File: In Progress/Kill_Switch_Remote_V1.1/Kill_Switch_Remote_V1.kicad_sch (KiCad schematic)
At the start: 56 parts, among them J1 USB_B_Micro, J2 S2B-PH-K-S(LF)(SN), J3 U.FL-R-SMT-1(10), Q2 UMH3N, SW4 AS11CH, U1 ESP32-PICO-MINI-02, U2 CP2102N-A02-GQFN28, U3 LP5912-3.3DRV, U4 MCP73871-2CC-Custom, U5 RFM95W-915S2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

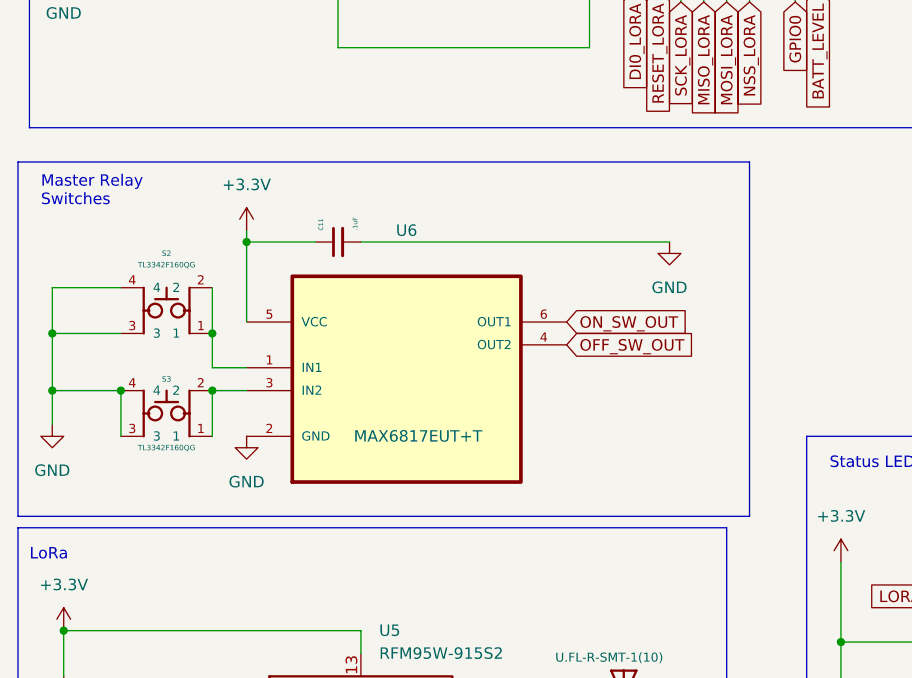
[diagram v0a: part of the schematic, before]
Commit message: Updating the Kill Switch Droid side
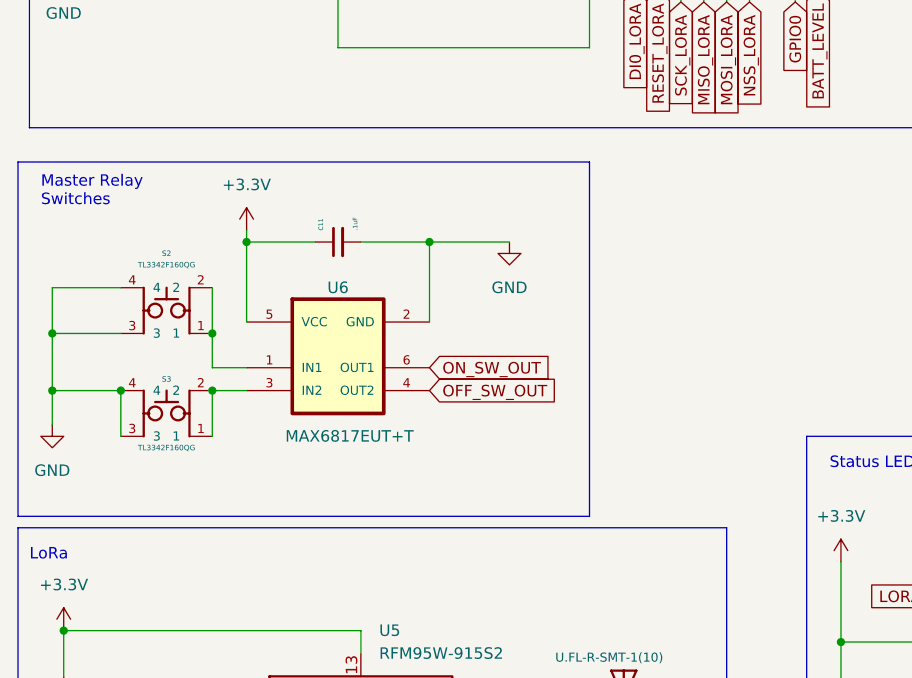
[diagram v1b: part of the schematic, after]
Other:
- moved on the sheet: U6
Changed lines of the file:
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@@
   (junction (at 104.14 152.4) (diameter 0) (color 0 0 0 0)
   )
+  (junction (at 58.42 107.95) (diameter 0) (color 0 0 0 0)
+  )
   (junction (at 35.56 68.58) (diameter 0) (color 0 0 0 0)
   )
@@
     (stroke (width 0) (type default) (color 0 0 0 0))
   )
-  (polyline (pts (xy 12.7 99.06) (xy 93.98 99.06))
+  (polyline (pts (xy 12.7 99.06) (xy 76.2 99.06))
     (stroke (width 0) (type default) (color 0 0 0 0))
   )
@@
     (stroke (width 0) (type default) (color 0 0 0 0))
   )
+  (wire (pts (xy 58.42 107.95) (xy 67.31 107.95))
+    (stroke (width 0) (type default) (color 0 0 0 0))
+  )
   (wire (pts (xy 237.49 66.04) (xy 237.49 71.12))
     (stroke (width 0) (type default) (color 0 0 0 0))
@@
     (stroke (width 0) (type default) (color 0 0 0 0))
   )
+  (wire (pts (xy 58.42 107.95) (xy 58.42 116.84))
+    (stroke (width 0) (type default) (color 0 0 0 0))
+  )
   (wire (pts (xy 48.26 21.59) (xy 48.26 36.83))
     (stroke (width 0) (type default) (color 0 0 0 0))
@@
     (stroke (width 0) (type default) (color 0 0 0 0))
   )
-  (polyline (pts (xy 12.7 138.43) (xy 93.98 138.43))
+  (polyline (pts (xy 12.7 138.43) (xy 76.2 138.43))
     (stroke (width 0) (type default) (color 0 0 0 0))
   )
@@
     (stroke (width 0) (type default) (color 0 0 0 0))
   )
-  (wire (pts (xy 50.8 107.95) (xy 85.09 107.95))
+  (wire (pts (xy 50.8 107.95) (xy 58.42 107.95))
     (stroke (width 0) (type default) (color 0 0 0 0))
   )
@@
     (stroke (width 0) (type default) (color 0 0 0 0))
   )
-  (polyline (pts (xy 93.98 138.43) (xy 93.98 99.06))
+  (polyline (pts (xy 76.2 138.43) (xy 76.2 99.06))
     (stroke (width 0) (type default) (color 0 0 0 0))
   )
@@
     )
   )
-  (global_label "OFF_SW_OUT" (shape input) (at 73.66 119.38 0) (fields_autoplaced)
+  (global_label "OFF_SW_OUT" (shape input) (at 58.42 124.46 0) (fields_autoplaced)
     (effects (font (size 1.27 1.27)) (justify left))
-    (property "Intersheet References" "${INTERSHEET_REFS}" (id 0) (at 87.8055 119.3006 0)
+    (property "Intersheet References" "${INTERSHEET_REFS}" (id 0) (at 72.5655 124.3806 0)
       (effects (font (size 1.27 1.27)) (justify left) hide)
     )
@@
     )
   )
-  (global_label "ON_SW_OUT" (shape input) (at 73.66 116.84 0) (fields_autoplaced)
+  (global_label "ON_SW_OUT" (shape input) (at 58.42 121.92 0) (fields_autoplaced)
     (effects (font (size 1.27 1.27)) (justify left))
-    (property "Intersheet References" "${INTERSHEET_REFS}" (id 0) (at 86.9588 116.7606 0)
+    (property "Intersheet References" "${INTERSHEET_REFS}" (id 0) (at 71.7188 121.8406 0)
       (effects (font (size 1.27 1.27)) (justify left) hide)
     )
@@
     (pin "2")
   )
-  (symbol (lib_id "power:GND") (at 38.1 129.54 0) (unit 1)
-    (in_bom yes) (on_board yes) (fields_autoplaced)
-    (property "Reference" "#PWR0143" (id 0) (at 38.1 135.89 0)
-      (effects (font (size 1.27 1.27)) hide)
-    )
-    (property "Value" "GND" (id 1) (at 38.1 134.62 0))
-    (property "Footprint" "" (id 2) (at 38.1 129.54 0)
-      (effects (font (size 1.27 1.27)) hide)
-    )
-    (property "Datasheet" "" (id 3) (at 38.1 129.54 0)
-      (effects (font (size 1.27 1.27)) hide)
-    )
-    (pin "1")
-  )
   (symbol (lib_id "power:GND") (at 151.13 172.72 0) (unit 1)
     (in_bom yes) (on_board yes)
@@
     (pin "1")
   )
-  (symbol (lib_id "Custom:MAX6817EUT+T") (at 55.88 119.38 0) (unit 1)
+  (symbol (lib_id "Custom:MAX6817EUT+T") (at 48.26 119.38 0) (unit 1)
     (in_bom yes) (on_board yes)
-    (property "Reference" "U6" (id 0) (at 55.88 106.68 0))
-    (property "Value" "MAX6817EUT+T" (id 1) (at 57.15 129.54 0))
-    (property "Footprint" "SOT95P280X145-6N" (id 2) (at 55.88 119.38 0)
+    (property "Reference" "U6" (id 0) (at 48.26 113.03 0))
+    (property "Value" "MAX6817EUT+T" (id 1) (at 49.53 129.54 0))
+    (property "Footprint" "SOT95P280X145-6N" (id 2) (at 48.26 119.38 0)
       (effects (font (size 1.27 1.27)) (justify bottom) hide)
     )
-    (property "Datasheet" "https://www.analog.com/media/en/technical-documentation/data-sheets/MAX6816-MAX6818.pdf" (id 3) (at 55.88 119.38 0)
+    (property "Datasheet" "https://www.analog.com/media/en/technical-documentation/data-sheets/MAX6816-MAX6818.pdf" (id 3) (at 48.26 119.38 0)
       (effects (font (size 1.27 1.27)) hide)
     )
-    (property "PACKAGE" "SOT23-6" (id 4) (at 55.88 119.38 0)
+    (property "PACKAGE" "SOT23-6" (id 4) (at 48.26 119.38 0)
       (effects (font (size 1.27 1.27)) (justify bottom) hide)
     )
-    (property "MPN" "MAX6817EUT+T" (id 5) (at 55.88 119.38 0)
+    (property "MPN" "MAX6817EUT+T" (id 5) (at 48.26 119.38 0)
       (effects (font (size 1.27 1.27)) (justify bottom) hide)
     )
-    (property "OC_NEWARK" "68K9458" (id 6) (at 55.88 119.38 0)
+    (property "OC_NEWARK" "68K9458" (id 6) (at 48.26 119.38 0)
       (effects (font (size 1.27 1.27)) (justify bottom) hide)
     )
-    (property "OC_FARNELL" "1299771" (id 7) (at 55.88 119.38 0)
+    (property "OC_FARNELL" "1299771" (id 7) (at 48.26 119.38 0)
       (effects (font (size 1.27 1.27)) (justify bottom) hide)
     )
-    (property "SUPPLIER" "Maxim" (id 8) (at 55.88 119.38 0)
+    (property "SUPPLIER" "Maxim" (id 8) (at 48.26 119.38 0)
       (effects (font (size 1.27 1.27)) (justify bottom) hide)
     )
@@
     (pin "2")
   )
-  (symbol (lib_id "power:GND") (at 85.09 107.95 0) (unit 1)
+  (symbol (lib_id "power:GND") (at 67.31 107.95 0) (unit 1)
     (in_bom yes) (on_board yes) (fields_autoplaced)
-    (property "Reference" "#PWR0127" (id 0) (at 85.09 114.3 0)
+    (property "Reference" "#PWR0127" (id 0) (at 67.31 114.3 0)
       (effects (font (size 1.27 1.27)) hide)
     )
-    (property "Value" "GND" (id 1) (at 85.09 113.03 0))
-    (property "Footprint" "" (id 2) (at 85.09 107.95 0)
+    (property "Value" "GND" (id 1) (at 67.31 113.03 0))
+    (property "Footprint" "" (id 2) (at 67.31 107.95 0)
       (effects (font (size 1.27 1.27)) hide)
     )
-    (property "Datasheet" "" (id 3) (at 85.09 107.95 0)
+    (property "Datasheet" "" (id 3) (at 67.31 107.95 0)
       (effects (font (size 1.27 1.27)) hide)
     )
@@
       (reference "#PWR0142") (unit 1) (value "GND") (footprint "")
     )
-    (path "/29c27ba3-a492-44ef-9417-774b5144448a"
-      (reference "#PWR0143") (unit 1) (value "GND") (footprint "")
-    )
     (path "/1e10f6a7-f66e-43cd-a1bd-d7754ef94760"

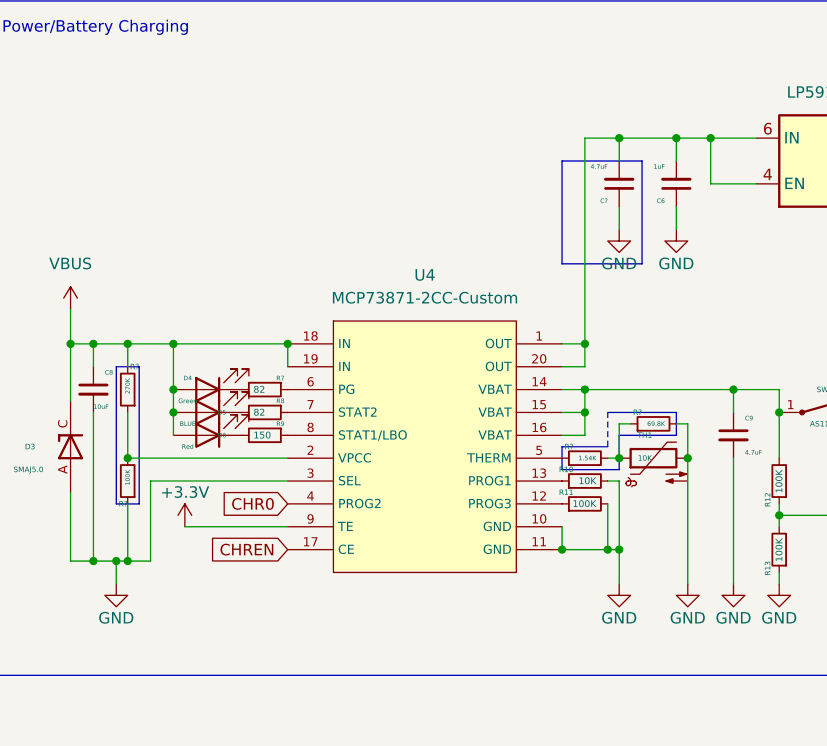
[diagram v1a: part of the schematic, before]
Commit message: Updates to the kill switches
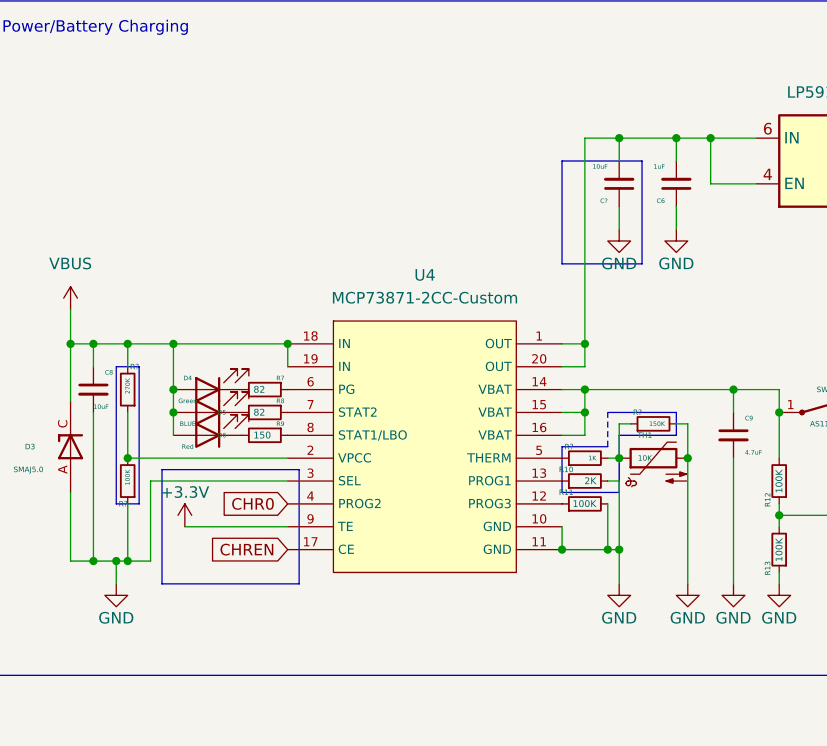
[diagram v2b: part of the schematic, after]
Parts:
- C?: value 4.7uF -> 10uF
- R10: value 10K -> 2K
- R?: value 1.54K -> 1K
- R?: value 69.8K -> 150K
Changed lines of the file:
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@@
     (stroke (width 0) (type default) (color 0 0 0 0))
   )
-  (polyline (pts (xy 231.14 140.97) (xy 224.79 140.97))
+  (polyline (pts (xy 231.14 143.51) (xy 224.79 143.51))
     (stroke (width 0) (type default) (color 0 0 0 0))
   )
@@
     (stroke (width 0) (type default) (color 0 0 0 0))
   )
+  (polyline (pts (xy 195.58 153.67) (xy 195.58 140.97))
+    (stroke (width 0) (type default) (color 0 0 0 0))
+  )
   (wire (pts (xy 232.41 77.47) (xy 232.41 80.01))
     (stroke (width 0) (type default) (color 0 0 0 0))
@@
     (stroke (width 0) (type default) (color 0 0 0 0))
   )
+  (polyline (pts (xy 180.34 142.24) (xy 180.34 140.97))
+    (stroke (width 0) (type default) (color 0 0 0 0))
+  )
   (wire (pts (xy 21.59 41.91) (xy 21.59 46.99))
     (stroke (width 0) (type default) (color 0 0 0 0))
@@
     (stroke (width 0) (type default) (color 0 0 0 0))
   )
-  (polyline (pts (xy 231.14 137.16) (xy 231.14 140.97))
+  (polyline (pts (xy 231.14 137.16) (xy 231.14 143.51))
     (stroke (width 0) (type default) (color 0 0 0 0))
   )
@@
     (stroke (width 0) (type default) (color 0 0 0 0))
   )
+  (polyline (pts (xy 180.34 142.24) (xy 180.34 153.67))
+    (stroke (width 0) (type default) (color 0 0 0 0))
+  )
   (wire (pts (xy 16.51 118.11) (xy 16.51 124.46))
     (stroke (width 0) (type default) (color 0 0 0 0))
@@
     (stroke (width 0) (type default) (color 0 0 0 0))
   )
+  (polyline (pts (xy 180.34 153.67) (xy 195.58 153.67))
+    (stroke (width 0) (type default) (color 0 0 0 0))
+  )
   (wire (pts (xy 248.92 146.05) (xy 248.92 147.32))
     (stroke (width 0) (type default) (color 0 0 0 0))
@@
     (stroke (width 0) (type default) (color 0 0 0 0))
   )
+  (polyline (pts (xy 180.34 140.97) (xy 195.58 140.97))
+    (stroke (width 0) (type default) (color 0 0 0 0))
+  )
   (wire (pts (xy 232.41 69.85) (xy 232.41 71.12))
     (stroke (width 0) (type default) (color 0 0 0 0))
@@
     (stroke (width 0) (type default) (color 0 0 0 0))
   )
-  (polyline (pts (xy 224.79 138.43) (xy 224.79 140.97))
+  (polyline (pts (xy 224.79 138.43) (xy 224.79 143.51))
     (stroke (width 0) (type default) (color 0 0 0 0))
   )
@@
   (symbol (lib_id "power:GND") (at 231.14 114.3 0) (unit 1)
     (in_bom yes) (on_board yes)
-    (property "Reference" "#PWR?" (id 0) (at 231.14 120.65 0)
+    (property "Reference" "#PWR0110" (id 0) (at 231.14 120.65 0)
       (effects (font (size 1.27 1.27)) hide)
     )
@@
   (symbol (lib_id "power:+3.3V") (at 182.88 147.32 0) (unit 1)
     (in_bom yes) (on_board yes)
-    (property "Reference" "#PWR?" (id 0) (at 182.88 151.13 0)
+    (property "Reference" "#PWR0124" (id 0) (at 182.88 151.13 0)
       (effects (font (size 1.27 1.27)) hide)
     )
@@
       (effects (font (size 0.6 0.6)) (justify left))
     )
-    (property "Value" "1.54K" (id 1) (at 228.5999 139.7 90)
+    (property "Value" "1K" (id 1) (at 228.5999 139.7 90)
       (effects (font (size 0.5 0.5)) (justify left))
     )
@@
       (effects (font (size 0.6 0.6)) (justify left))
     )
-    (property "Value" "69.8K" (id 1) (at 236.2199 135.89 90)
+    (property "Value" "150K" (id 1) (at 236.2199 135.89 90)
       (effects (font (size 0.5 0.5)) (justify left))
     )
@@
       (effects (font (size 0.6 0.6)) (justify left))
     )
-    (property "Value" "10K" (id 1) (at 228.5999 142.24 90)
+    (property "Value" "2K" (id 1) (at 228.5999 142.24 90)
       (effects (font (size 0.75 0.75)) (justify left))
     )
@@
       (effects (font (size 0.5 0.5)) (justify left))
     )
-    (property "Value" "4.7uF" (id 1) (at 229.87 107.3087 0)
+    (property "Value" "10uF" (id 1) (at 229.87 107.3087 0)
       (effects (font (size 0.5 0.5)) (justify left))
     )
@@
       (reference "#PWR0109") (unit 1) (value "VBUS") (footprint "")
     )
+    (path "/1e10f6a7-f66e-43cd-a1bd-d7754ef94760"
+      (reference "#PWR0110") (unit 1) (value "GND") (footprint "")
+    )
     (path "/bad23856-16c5-4ca9-9cf1-3ff227aac12c"
       (reference "#PWR0111") (unit 1) (value "+3.3V") (footprint "")
@@
       (reference "#PWR0123") (unit 1) (value "+3.3V") (footprint "")
     )
+    (path "/4cb7e6c7-9ecc-4a50-8b46-a0cbea5b04a1"
+      (reference "#PWR0124") (unit 1) (value "+3.3V") (footprint "")
+    )
     (path "/f4f8ff7a-504e-4acb-b43a-4c7a2226ed1f"
       (reference "#PWR0125") (unit 1) (value "GND") (footprint "")
@@
       (reference "#PWR0142") (unit 1) (value "GND") (footprint "")
     )
-    (path "/1e10f6a7-f66e-43cd-a1bd-d7754ef94760"
-      (reference "#PWR?") (unit 1) (value "GND") (footprint "")
-    )
-    (path "/4cb7e6c7-9ecc-4a50-8b46-a0cbea5b04a1"
-      (reference "#PWR?") (unit 1) (value "+3.3V") (footprint "")
-    )
     (path "/533cca49-24cb-4acd-b769-43fedf45f7d4"
       (reference "C1") (unit 1) (value "10uF") (footprint "Capacitor_SMD:C_0805_2012Metric")
@@
     )
     (path "/b6a1b420-5923-4593-842a-f8492b29f0d0"
-      (reference "C?") (unit 1) (value "4.7uF") (footprint "Capacitor_SMD:C_0603_1608Metric")
+      (reference "C?") (unit 1) (value "10uF") (footprint "Capacitor_SMD:C_0603_1608Metric")
     )
     (path "/aced5076-6949-4319-92cc-c0f846e24a52"
@@
     )
     (path "/9d2c8602-7e31-495b-9277-6db28d0000b7"
-      (reference "R10") (unit 1) (value "10K") (footprint "Resistor_SMD:R_0402_1005Metric")
+      (reference "R10") (unit 1) (value "2K") (footprint "Resistor_SMD:R_0402_1005Metric")
     )
     (path "/42073a96-4292-460e-841b-30346db296ea"
@@
     )
     (path "/64ab4920-b4c9-41f2-b441-6c07e58717e2"
-      (reference "R?") (unit 1) (value "1.54K") (footprint "Resistor_SMD:R_0402_1005Metric")
+      (reference "R?") (unit 1) (value "1K") (footprint "Resistor_SMD:R_0402_1005Metric")
     )
     (path "/6bf1f89b-ea37-451a-a46b-79488777dde0"
-      (reference "R?") (unit 1) (value "69.8K") (footprint "Resistor_SMD:R_0402_1005Metric")
+      (reference "R?") (unit 1) (value "150K") (footprint "Resistor_SMD:R_0402_1005Metric")
     )
     (path "/ba9471bb-e888-4729-b27b-07f20ad69002"
